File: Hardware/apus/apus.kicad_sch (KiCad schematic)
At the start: 56 parts, among them J1 Conn_01x04_Socket, J3 Pyros, Q1 AO3401A, Q2 YJQ3622A, SW1 BOOT, U1 STM32WLE5CBUx, U2 XC6206P332MR, U3 MS5607-02BA, U4 W25Q16JVUXIQ, U6 BMI270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

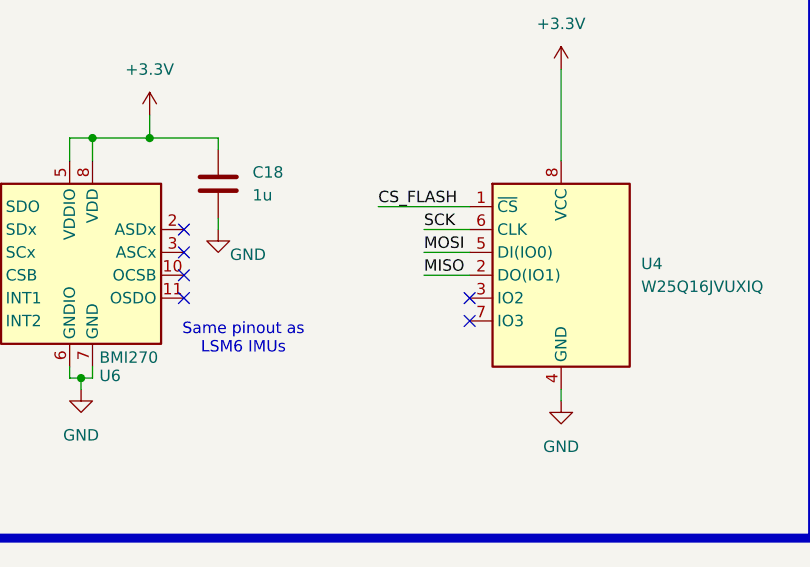
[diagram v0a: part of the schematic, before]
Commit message: APRS emulation testing, trying to get long packets working
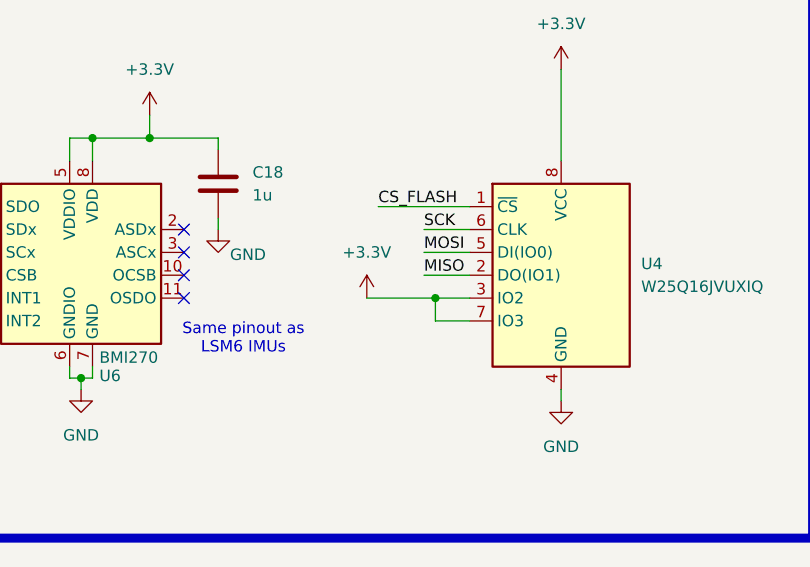
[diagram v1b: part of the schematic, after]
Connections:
- net +3.3V: now also U4.3 (IO2), U4.7 (IO3)
- no-connect marks 20 -> 18
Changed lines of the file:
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@@
 	)
 	(junction
+		(at 364.49 224.79)
+		(diameter 0)
+		(color 0 0 0 0)
+	)
+	(junction
 		(at 347.98 78.74)
 		(diameter 0)
@@
 	)
 	(no_connect
-		(at 368.3 224.79)
-	)
-	(no_connect
 		(at 336.55 217.17)
 	)
@@
 	)
 	(no_connect
-		(at 368.3 227.33)
-	)
-	(no_connect
 		(at 313.69 227.33)
 	)
@@
 	(wire
 		(pts
+			(xy 356.87 224.79) (xy 364.49 224.79)
+		)
+		(stroke
+			(width 0)
+			(type default)
+		)
+	)
+	(wire
+		(pts
 			(xy 314.96 68.58) (xy 314.96 78.74)
 		)
@@
 	(wire
 		(pts
+			(xy 364.49 227.33) (xy 368.3 227.33)
+		)
+		(stroke
+			(width 0)
+			(type default)
+		)
+	)
+	(wire
+		(pts
 			(xy 273.05 102.87) (xy 276.86 102.87)
 		)
@@
 	(wire
 		(pts
+			(xy 364.49 224.79) (xy 364.49 227.33)
+		)
+		(stroke
+			(width 0)
+			(type default)
+		)
+	)
+	(wire
+		(pts
 			(xy 382.27 158.75) (xy 382.27 161.29)
 		)
@@
 	(wire
 		(pts
+			(xy 364.49 224.79) (xy 368.3 224.79)
+		)
+		(stroke
+			(width 0)
+			(type default)
+		)
+	)
+	(wire
+		(pts
 			(xy 214.63 30.48) (xy 210.82 30.48)
 		)
@@
 					(unit 1)
 				)
+			)
+		)
+	)
+	(symbol
+		(lib_id "power:+3.3V")
+		(at 356.87 224.79 0)
+		(unit 1)
+		(exclude_from_sim no)
+		(in_bom yes)
+		(on_board yes)
+		(dnp no)
+		(fields_autoplaced yes)
+		(property "Reference" "#PWR046"
+			(at 356.87 228.6 0)
+			(effects
+				(font
+					(size 1.27 1.27)
+				)
+				(hide yes)
+			)
+		)
+		(property "Value" "+3.3V"
+			(at 356.87 219.71 0)
+			(effects
+				(font
+					(size 1.27 1.27)
+				)
+			)
+		)
+		(property "Footprint" ""
+			(at 356.87 224.79 0)
+			(effects
+				(font
+					(size 1.27 1.27)
+				)
+				(hide yes)
+			)
+		)
+		(property "Datasheet" ""
+			(at 356.87 224.79 0)
+			(effects
+				(font
+					(size 1.27 1.27)
+				)
+				(hide yes)
+			)
+		)
+		(property "Description" ""
+			(at 356.87 224.79 0)
+			(effects
+				(font
+					(size 1.27 1.27)
+				)
+				(hide yes)
+			)
+		)
+		(pin "1"
+		)
+		(instances
+			(project "apus"
+				(path "/77054b9a-0066-4e8e-8fb2-f8dc67a92039"
+					(reference "#PWR046")
+					(unit 1)
+				)
